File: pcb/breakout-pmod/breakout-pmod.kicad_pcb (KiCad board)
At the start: 4 copper layers, 88.9 x 99.3 mm, 13 parts, among them J1 FX18-120P-0.8SV20

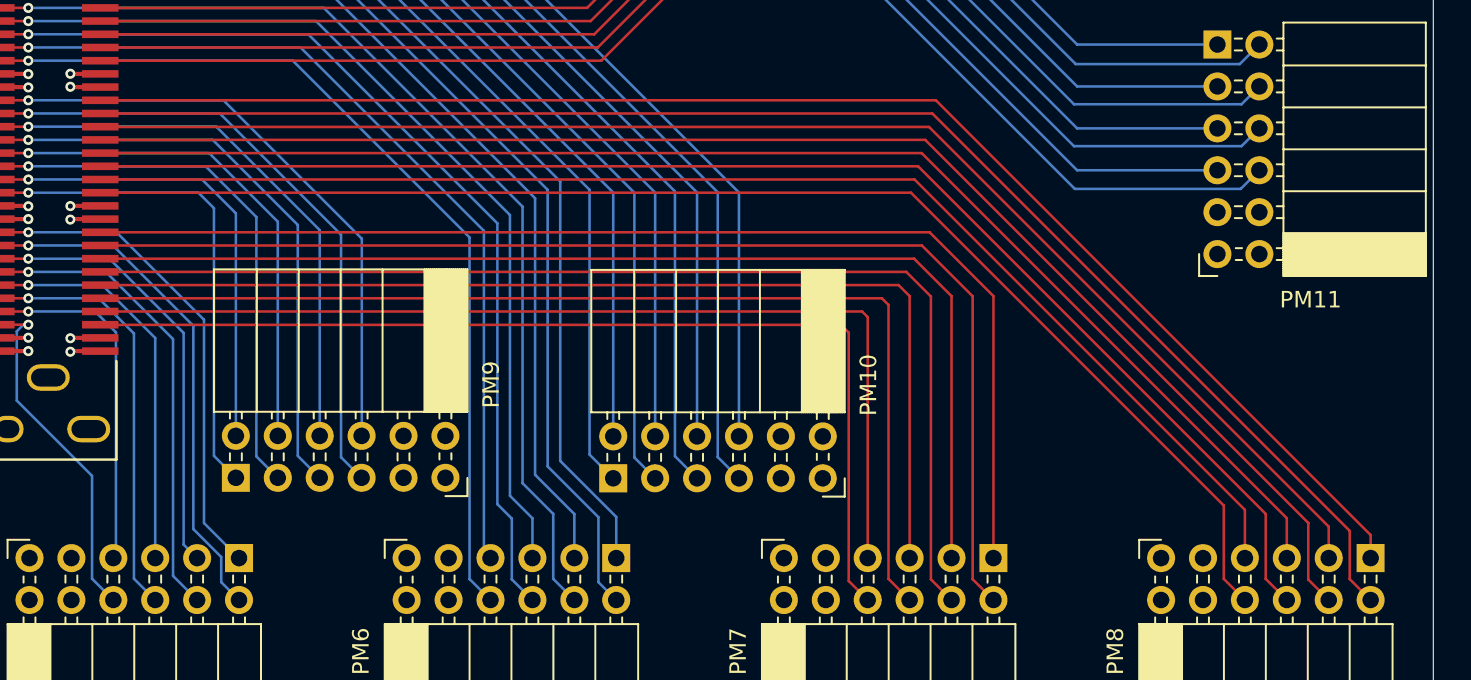
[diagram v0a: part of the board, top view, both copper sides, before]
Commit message: remove unused pmod symbol
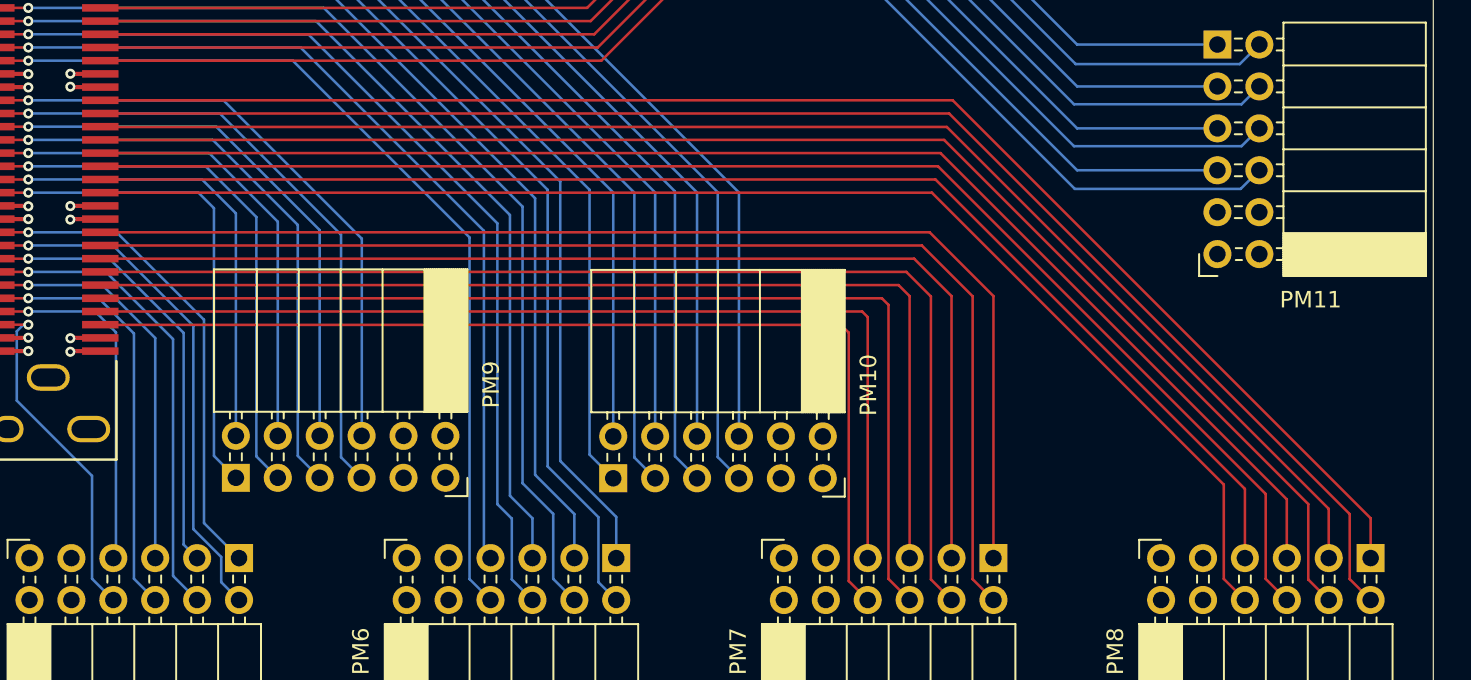
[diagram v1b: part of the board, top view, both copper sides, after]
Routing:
- net /IOL_17A: track 80.6 -> 81.3 mm
- net /IOL_17B: track 82.2 -> 82.9 mm
- net /IOL_14B: track 85.1 -> 85.8 mm
- net /IOL_13B: track 83.5 -> 84.2 mm
- net /IOL_13A: track 88.0 -> 88.7 mm
- net /IOL_12B: track 85.5 -> 86.1 mm
- net /IOL_12A: track 90.9 -> 91.5 mm
- net /IOL_10B: track 89.3 -> 89.9 mm
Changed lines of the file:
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@@
 	)
 	(segment
-		(start 103.145999 102.129999)
-		(end 126.36 125.344)
+		(start 53.150999 102.129999)
+		(end 104.288999 102.129999)
 		(width 0.156464)
 		(layer "F.Cu")
@@
 	)
 	(segment
-		(start 126.36 125.344)
+		(start 126.36 124.201)
 		(end 126.36 128.775)
 		(width 0.156464)
@@
 	)
 	(segment
-		(start 53.150999 102.129999)
-		(end 103.145999 102.129999)
+		(start 104.288999 102.129999)
+		(end 126.36 124.201)
 		(width 0.156464)
 		(layer "F.Cu")
@@
 	)
 	(segment
-		(start 122.52 124.552)
-		(end 122.52 127.475)
+		(start 53.150999 104.529996)
+		(end 103.767996 104.529996)
 		(width 0.156464)
 		(layer "F.Cu")
@@
 	)
 	(segment
-		(start 102.497996 104.529996)
-		(end 122.52 124.552)
+		(start 122.52 123.282)
+		(end 122.52 127.475)
 		(width 0.156464)
 		(layer "F.Cu")
@@
 	)
 	(segment
-		(start 53.150999 104.529996)
-		(end 102.497996 104.529996)
+		(start 103.767996 104.529996)
+		(end 122.52 123.282)
 		(width 0.156464)
 		(layer "F.Cu")
@@
 	)
 	(segment
-		(start 102.713998 103.729998)
-		(end 123.78 124.796)
+		(start 123.78 128.735)
+		(end 125.06 130.015)
 		(width 0.156464)
 		(layer "F.Cu")
@@
 	)
 	(segment
-		(start 123.78 124.796)
-		(end 123.78 128.735)
+		(start 103.920498 103.729998)
+		(end 123.78 123.5895)
 		(width 0.156464)
 		(layer "F.Cu")
@@
 	(segment
 		(start 53.150999 103.729998)
-		(end 102.713998 103.729998)
+		(end 103.920498 103.729998)
 		(width 0.156464)
 		(layer "F.Cu")
@@
 	)
 	(segment
-		(start 123.78 128.735)
-		(end 125.06 130.015)
+		(start 123.78 123.5895)
+		(end 123.78 128.735)
 		(width 0.156464)
 		(layer "F.Cu")
@@
 	)
 	(segment
-		(start 53.150999 102.929997)
-		(end 102.929997 102.929997)
+		(start 125.06 123.917)
+		(end 125.06 127.475)
 		(width 0.156464)
 		(layer "F.Cu")
@@
 	)
 	(segment
-		(start 125.06 125.06)
-		(end 125.06 127.475)
+		(start 53.150999 102.929997)
+		(end 104.072997 102.929997)
 		(width 0.156464)
 		(layer "F.Cu")
@@
 	)
 	(segment
-		(start 102.929997 102.929997)
-		(end 125.06 125.06)
+		(start 104.072997 102.929997)
+		(end 125.06 123.917)
 		(width 0.156464)
 		(layer "F.Cu")
@@
 	)
 	(segment
-		(start 53.150999 99.729998)
-		(end 103.793998 99.729998)
+		(start 130.14 125.06)
+		(end 130.14 127.475)
 		(width 0.156464)
 		(layer "F.Cu")
@@
 	)
 	(segment
-		(start 130.14 126.076)
-		(end 130.14 127.475)
+		(start 104.809998 99.729998)
+		(end 130.14 125.06)
 		(width 0.156464)
 		(layer "F.Cu")
@@
 	)
 	(segment
-		(start 103.793998 99.729998)
-		(end 130.14 126.076)
+		(start 53.150999 99.729998)
+		(end 104.809998 99.729998)
 		(width 0.156464)
 		(layer "F.Cu")
@@
 	)
 	(segment
-		(start 53.150999 100.529997)
-		(end 103.577997 100.529997)
+		(start 104.593997 100.529997)
+		(end 128.87 124.806)
 		(width 0.156464)
 		(layer "F.Cu")
@@
 	)
 	(segment
-		(start 103.577997 100.529997)
-		(end 128.87 125.822)
+		(start 53.150999 100.529997)
+		(end 104.593997 100.529997)
 		(width 0.156464)
 		(layer "F.Cu")
@@
 	)
 	(segment
-		(start 128.87 125.822)
+		(start 128.87 124.806)
 		(end 128.87 128.745)
 		(width 0.156464)
@@
 	)
 	(segment
-		(start 102.281997 105.329997)
-		(end 121.24 124.288)
+		(start 53.150999 105.329997)
+		(end 103.551997 105.329997)
 		(width 0.156464)
 		(layer "F.Cu")
@@
 	)
 	(segment
-		(start 121.24 128.735)
-		(end 122.52 130.015)
+		(start 121.24 123.018)
+		(end 121.24 128.735)
 		(width 0.156464)
 		(layer "F.Cu")
@@
 	)
 	(segment
-		(start 53.150999 105.329997)
-		(end 102.281997 105.329997)
+		(start 121.24 128.735)
+		(end 122.52 130.015)
 		(width 0.156464)
 		(layer "F.Cu")
@@
 	)
 	(segment
-		(start 121.24 124.288)
-		(end 121.24 128.735)
+		(start 103.551997 105.329997)
+		(end 121.24 123.018)
 		(width 0.156464)
 		(layer "F.Cu")
@@
 	)
 	(segment
-		(start 103.378 101.346)
-		(end 127.6 125.568)
+		(start 127.6 124.4885)
+		(end 127.6 127.475)
 		(width 0.156464)
 		(layer "F.Cu")
@@
 	(segment
 		(start 54.043301 101.346)
-		(end 103.378 101.346)
+		(end 104.4575 101.346)
 		(width 0.156464)
 		(layer "F.Cu")
@@
 	)
 	(segment
-		(start 127.6 125.568)
-		(end 127.6 127.475)
+		(start 104.4575 101.346)
+		(end 127.6 124.4885)
 		(width 0.156464)
 		(layer "F.Cu")

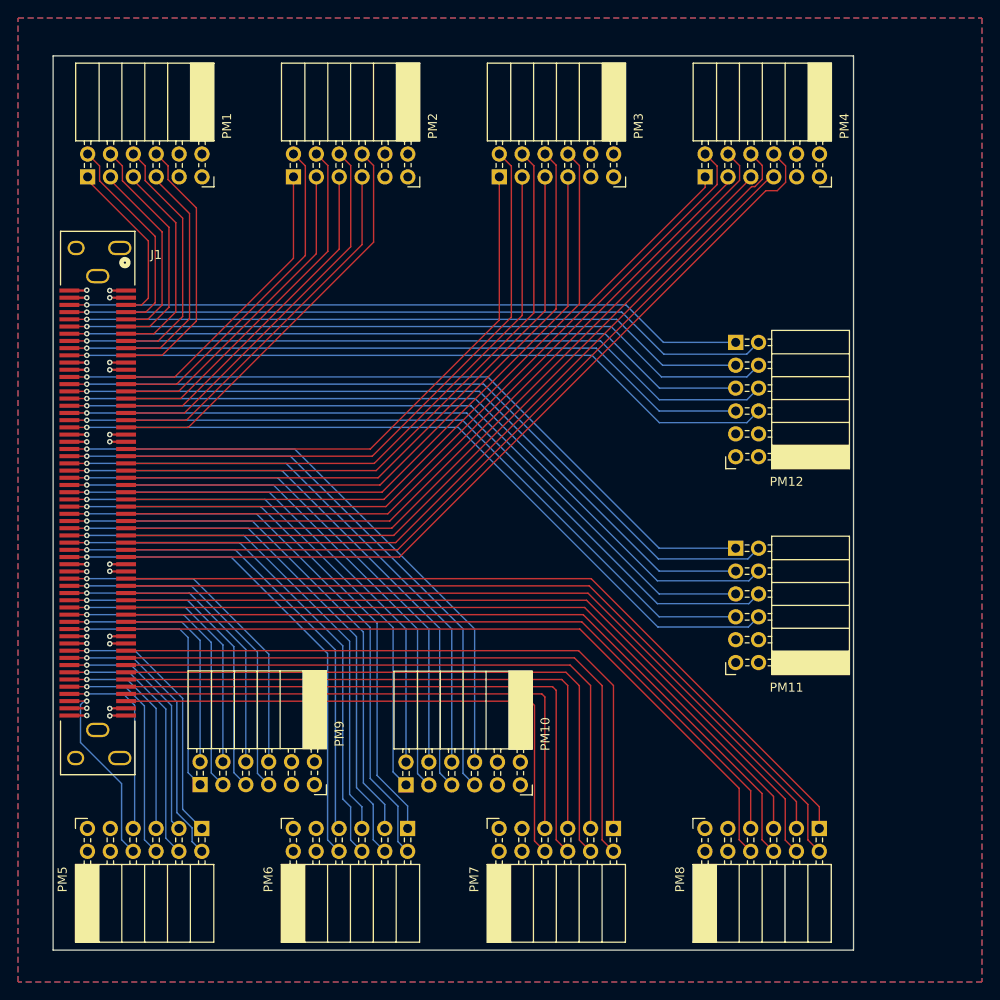
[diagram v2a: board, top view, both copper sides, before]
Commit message: [pass] breakout passthrough
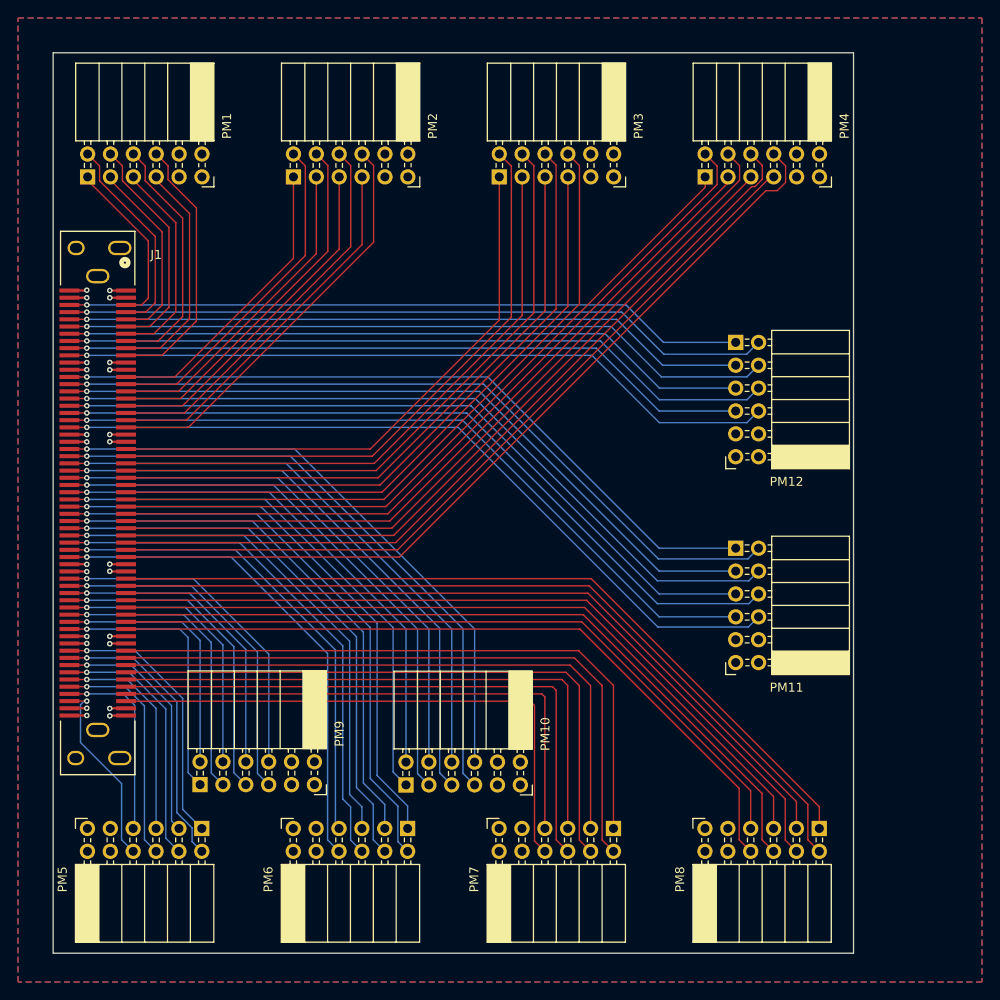
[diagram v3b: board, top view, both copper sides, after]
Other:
- board size 88.9 x 99.3 mm -> 88.9 x 100 mm
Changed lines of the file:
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@@
 	)
 	(gr_rect
-		(start 45.05 41.675)
-		(end 133.94 140.985)
+		(start 45.05 41.33)
+		(end 133.94 141.33)
 		(stroke
 			(width 0.05)

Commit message: [pmod] ab based labels
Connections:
- net /IOB_102 renamed /HG_08
- net /IOB_56 renamed /LK_08
- net /IOB_57 renamed /LK_07
- net /IOB_61 renamed /LK_06
- net /IOB_63 renamed /LK_05
- net /IOB_64 renamed /LK_04
- net /IOB_71 renamed /LK_03
- net /IOB_72 renamed /LK_02
- net /IOB_73 renamed /LK_01
- net /IOB_79 renamed /JI_08
- net /IOB_80 renamed /JI_07
- net /IOB_81 renamed /JI_06
- net /IOB_82 renamed /JI_05
- net /IOB_91 renamed /JI_04
- net /IOB_94 renamed /JI_03
- net /IOB_95 renamed /JI_02
- net /IOB_96 renamed /JI_01
- net /IOL_10A renamed /GH_08
- net /IOL_10B renamed /IJ_01
- net /IOL_12A renamed /IJ_02
- net /IOL_12B renamed /IJ_03
- net /IOL_13A renamed /IJ_04
- net /IOL_13B renamed /IJ_05
- net /IOL_14B renamed /IJ_06
- net /IOL_17A renamed /IJ_07
- net /IOL_17B renamed /IJ_08
- net /IOL_18A renamed /KL_01
- net /IOL_18B renamed /KL_02
- net /IOL_23A renamed /KL_03
- net /IOL_23B renamed /KL_04
- net /IOL_24A renamed /KL_05
- net /IOL_24B renamed /KL_06
- net /IOL_25A renamed /KL_07
- net /IOL_25B renamed /KL_08
- net /IOL_4A renamed /GH_02
- net /IOL_4B renamed /GH_03
- net /IOL_5A renamed /GH_04
- net /IOL_5B renamed /GH_05
- net /IOL_8A renamed /GH_06
- net /IOL_8B renamed /GH_07
- net /IOR_109 renamed /HG_07
- net /IOR_110 renamed /HG_06
- net /IOR_111 renamed /HG_05
- net /IOR_112 renamed /HG_04
- net /IOR_114 renamed /HG_03
- net /IOR_115 renamed /HG_02
- net /IOR_116 renamed /HG_01
- net /IOR_117 renamed /FE_08
- net /IOR_118 renamed /FE_07
- net /IOR_119 renamed /FE_06
- net /IOR_120 renamed /FE_05
- net /IOR_128 renamed /FE_04
- net /IOR_136 renamed /FE_03
- net /IOR_137 renamed /FE_02
- net /IOR_138 renamed /FE_01
- net /IOR_139 renamed /DC_08
- net /IOR_140 renamed /DC_07
- net /IOR_141 renamed /DC_06
- net /IOR_144 renamed /DC_05
- net /IOR_146 renamed /DC_04
- net /IOR_147 renamed /DC_03
- net /IOR_148 renamed /DC_02
- net /IOR_152 renamed /DC_01
- net /IOR_160 renamed /BA_08
- net /IOR_161 renamed /BA_07
- net /IOR_164 renamed /BA_06
- net /IOR_165 renamed /BA_05
- net /IOR_166 renamed /BA_04
- net /IOR_167 renamed /BA_03
- net /IOT_168 renamed /BA_02
- net /IOT_169 renamed /BA_01
- net /IOT_170 renamed /CD_08
- net /IOT_171 renamed /CD_07
- net /IOT_172 renamed /CD_06
- net /IOT_173 renamed /CD_05
- net /IOT_174 renamed /CD_04
- net /IOT_177 renamed /CD_03
- net /IOT_178 renamed /CD_02
- net /IOT_179 renamed /CD_01
- net /IOT_181 renamed /AB_08
- net /IOT_190 renamed /AB_07
- net /IOT_191 renamed /AB_06
- net /IOT_192 renamed /AB_05
- net /IOT_197 renamed /AB_04
- net /IOT_198 renamed /AB_03
- net /IOT_206 renamed /AB_02
- net /IOT_212 renamed /AB_01
- net /IOT_213 renamed /EF_01
- net /IOT_214 renamed /EF_02
- net /IOT_215 renamed /EF_03
- net /IOT_216 renamed /EF_04
- net /IOT_217 renamed /EF_05
- net /IOT_219 renamed /EF_06
- net /IOT_220 renamed /EF_07
- net /IOT_221 renamed /EF_08
- net /IOT_222 renamed /GH_01

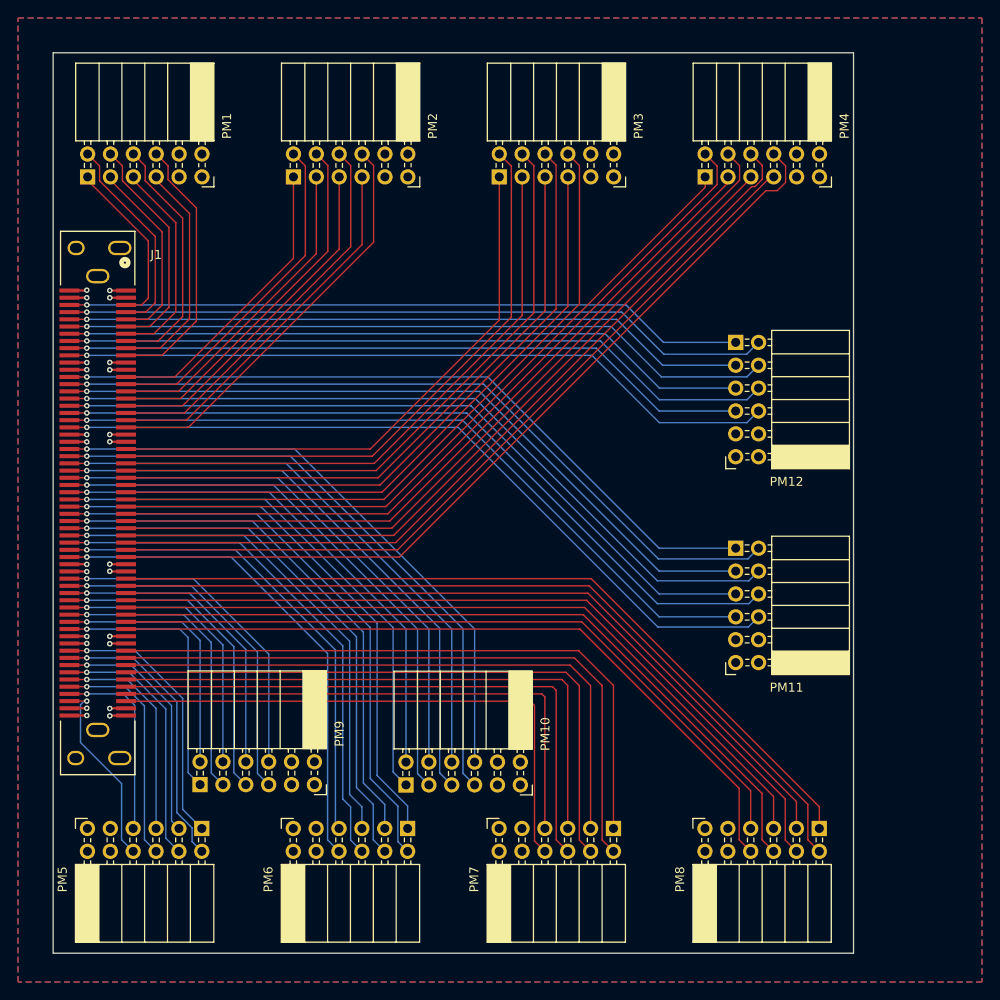
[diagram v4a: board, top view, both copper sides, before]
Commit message: [pmod] silkscreen labels
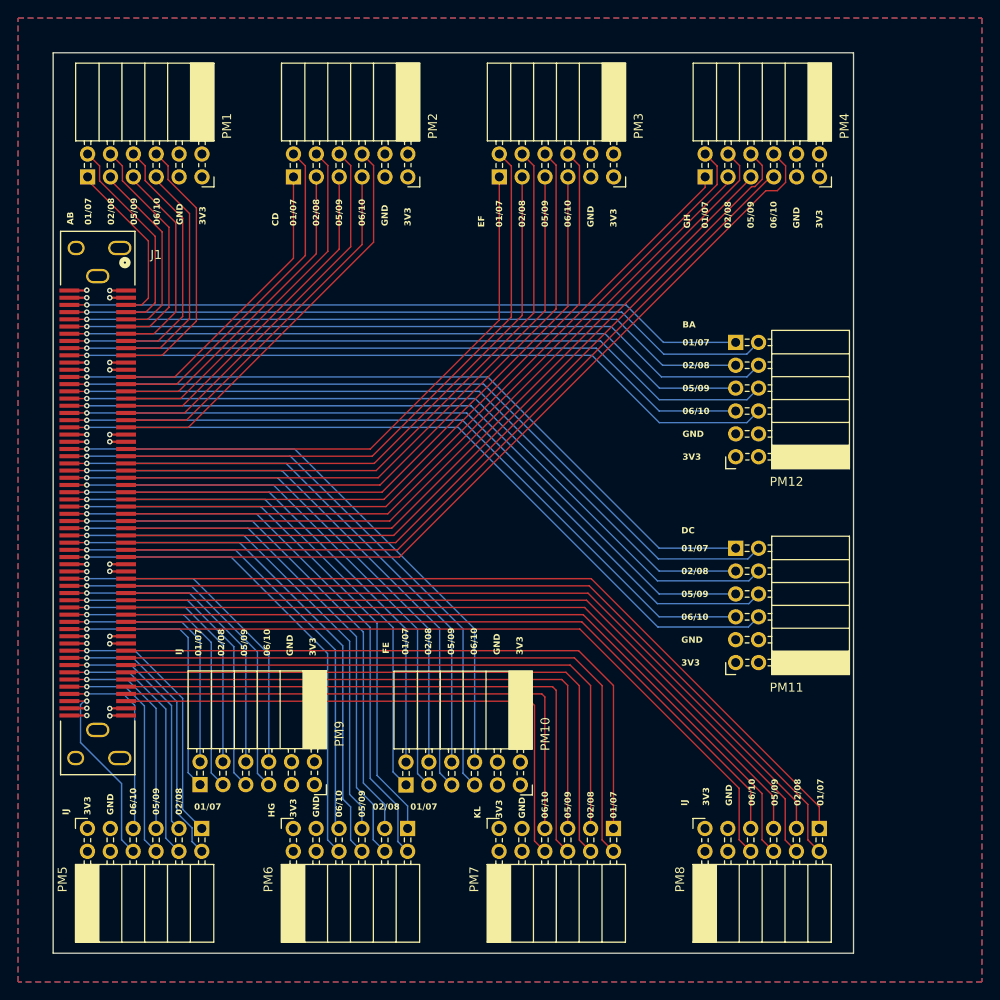
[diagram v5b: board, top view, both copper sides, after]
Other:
- board text added: "01/07"
- board text added: "02/08"
- board text added: "05/09"
- board text added: "06/10"
- board text added: "3V3"
- board text added: "AB"
- board text added: "BA"
- board text added: "CD"
- board text added: "DC"
- board text added: "EF"
- board text added: "FE"
- board text added: "GH"
- board text added: "GND"
- board text added: "HG"
- board text added: "IJ"
- board text added: "KL"

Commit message: [pmod] fix order of ef and gh pmod
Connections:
- J1 pad 24: /EF_02 -> /EF_05
- J1 pad 25: /EF_03 -> /EF_02
- J1 pad 26: /EF_04 -> /EF_06
- J1 pad 27: /EF_05 -> /EF_03
- J1 pad 28: /EF_06 -> /EF_07
- J1 pad 29: /EF_07 -> /EF_04
- J1 pad 32: /GH_02 -> /GH_05
- J1 pad 33: /GH_03 -> /GH_02
- J1 pad 34: /GH_04 -> /GH_06
- J1 pad 35: /GH_05 -> /GH_03
- J1 pad 36: /GH_06 -> /GH_07
- J1 pad 37: /GH_07 -> /GH_04
- PM3 pad 2: /EF_03 -> /EF_02
- PM3 pad 3: /EF_05 -> /EF_03
- PM3 pad 4: /EF_07 -> /EF_04
- PM3 pad 7: /EF_02 -> /EF_05
- PM3 pad 8: /EF_04 -> /EF_06
- PM3 pad 9: /EF_06 -> /EF_07
- PM4 pad 2: /GH_03 -> /GH_02
- PM4 pad 3: /GH_05 -> /GH_03
- PM4 pad 4: /GH_07 -> /GH_04
- PM4 pad 7: /GH_02 -> /GH_05
- PM4 pad 8: /GH_04 -> /GH_06
- PM4 pad 9: /GH_06 -> /GH_07
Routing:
- net /GH_03: track 82.4 -> 85.8 mm
- net /GH_06: track 90.7 -> 87.6 mm
- net /EF_03: track 66.2 -> 69.1 mm
- net /EF_06: track 73.6 -> 70.7 mm
- net /GH_02: track 84.7 -> 82.4 mm
- net /GH_07: track 88.7 -> 90.7 mm
- net /EF_02: track 67.9 -> 66.2 mm
- net /EF_07: track 72.0 -> 73.6 mm
- net /EF_04: track 70.7 -> 72.0 mm
- net /EF_05: track 69.1 -> 67.9 mm
- net /GH_04: track 87.6 -> 88.7 mm
- net /GH_05: track 85.8 -> 84.7 mm

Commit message: [pmod] fix order of CD pmod
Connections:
- J1 pad 14: /CD_02 -> /CD_05
- J1 pad 15: /CD_03 -> /CD_02
- J1 pad 16: /CD_04 -> /CD_06
- J1 pad 17: /CD_05 -> /CD_03
- J1 pad 18: /CD_06 -> /CD_07
- J1 pad 19: /CD_07 -> /CD_04
- PM2 pad 2: /CD_03 -> /CD_02
- PM2 pad 3: /CD_05 -> /CD_03
- PM2 pad 4: /CD_07 -> /CD_04
- PM2 pad 7: /CD_02 -> /CD_05
- PM2 pad 8: /CD_04 -> /CD_06
- PM2 pad 9: /CD_06 -> /CD_07
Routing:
- net /CD_03: track 36.0 -> 38.9 mm
- net /CD_06: track 43.4 -> 40.5 mm
- net /CD_02: track 37.6 -> 36.0 mm
- net /CD_07: track 41.8 -> 43.4 mm
- net /CD_04: track 40.5 -> 41.8 mm
- net /CD_05: track 38.9 -> 37.6 mm
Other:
- board text added: "01/05"
- board text added: "02/06"
- board text added: "03/07"
- board text added: "04/08"
